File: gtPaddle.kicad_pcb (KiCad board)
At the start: 2 copper layers, 139.7 x 57.2 mm, 24 parts, among them IC1 74157N

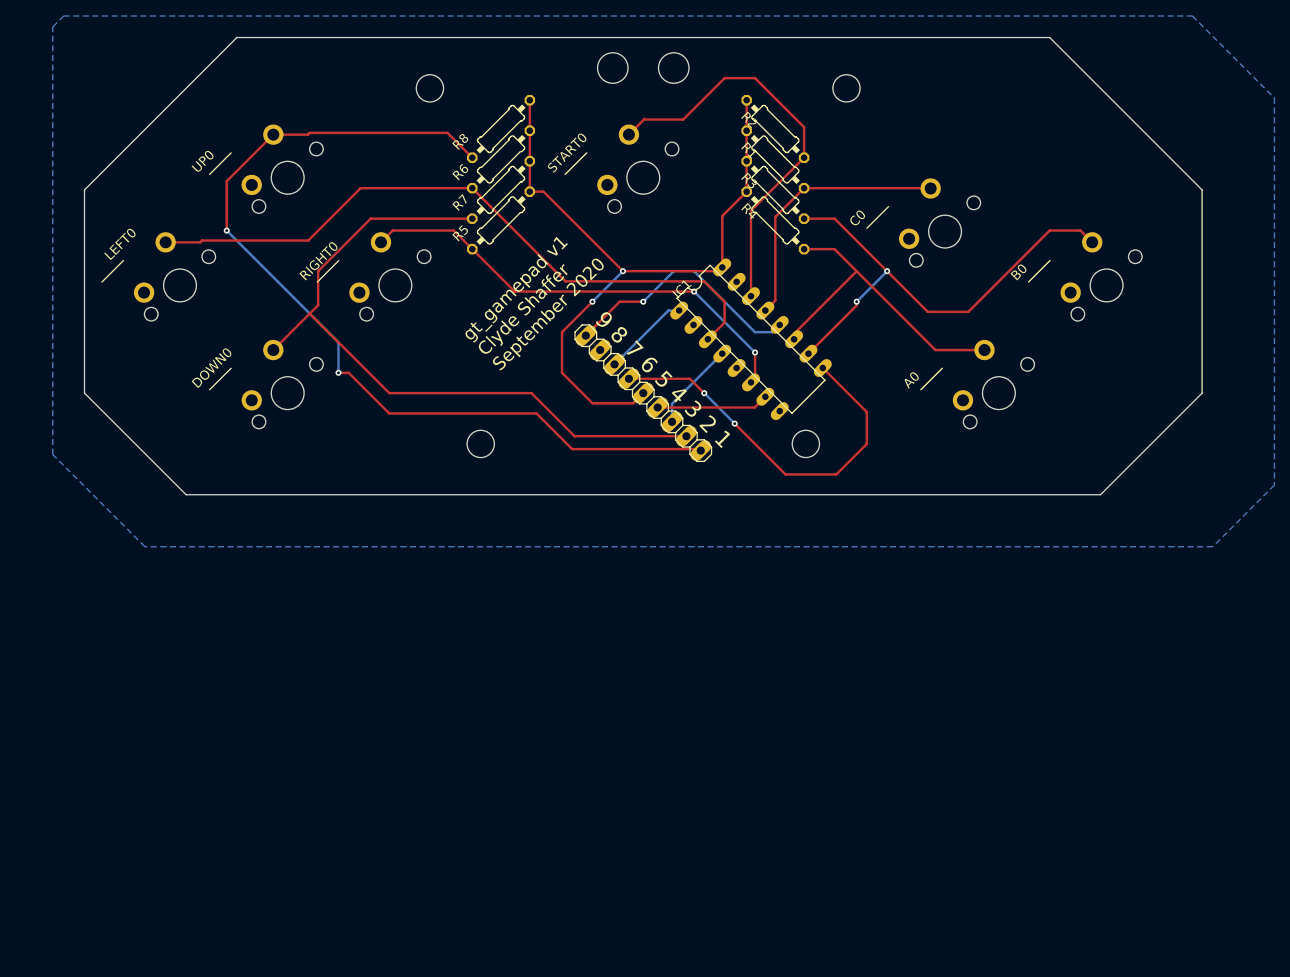
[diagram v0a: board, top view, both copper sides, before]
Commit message: start removing old pcb edits
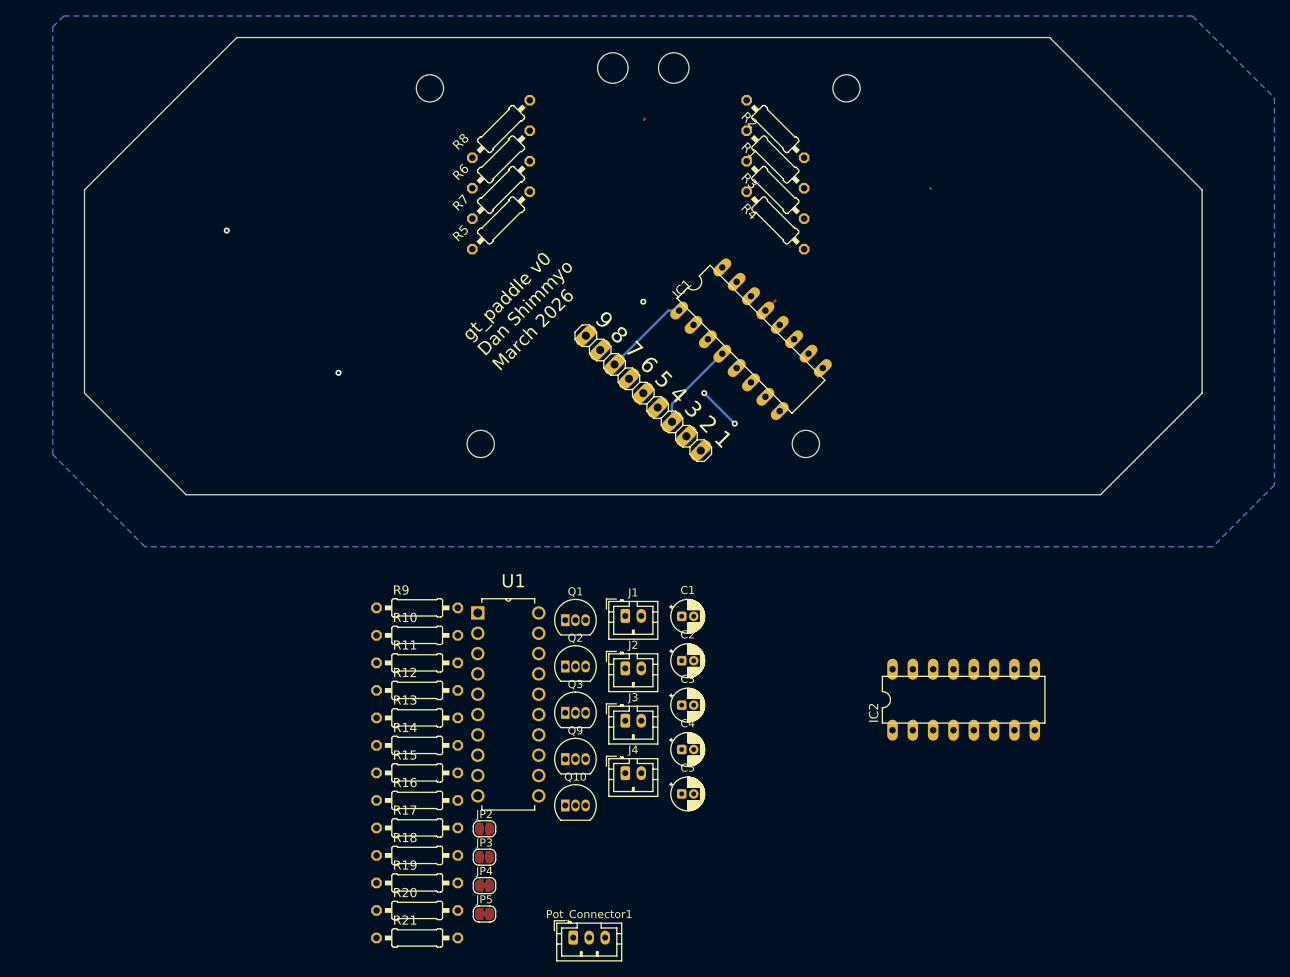
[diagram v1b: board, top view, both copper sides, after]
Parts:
- removed A0, B0, C0, DOWN0, LEFT0, RIGHT0, START0, UP0: CHERRY_MX, gpad1:CHERRY_MX
- added C1: 220pF, Capacitor_THT:CP_Radial_D4.0mm_P1.50mm, F.Cu at (148.4, 139.4)
- added C2: .1µF, Capacitor_THT:CP_Radial_D4.0mm_P1.50mm, F.Cu at (148.4, 144.9)
- added C3: .1µF, Capacitor_THT:CP_Radial_D4.0mm_P1.50mm, F.Cu at (148.4, 150.5)
- added C4: .1µF, Capacitor_THT:CP_Radial_D4.0mm_P1.50mm, F.Cu at (148.4, 156.0)
- added C5: .1µF, Capacitor_THT:CP_Radial_D4.0mm_P1.50mm, F.Cu at (148.4, 161.6)
- added IC2: 74157N, gpad1:DIL16, F.Cu at (183.7, 149.8)
- added J1: Conn_01x02_Pin, Connector_JST:JST_PH_B2B-PH-K_1x02_P2.00mm_Vertical, F.Cu at (141.4, 139.3)
- added J2: Conn_01x02_Pin, Connector_JST:JST_PH_B2B-PH-K_1x02_P2.00mm_Vertical, F.Cu at (141.4, 145.9)
- added J3: Conn_01x02_Pin, Connector_JST:JST_PH_B2B-PH-K_1x02_P2.00mm_Vertical, F.Cu at (141.4, 152.4)
- added J4: Conn_01x02_Pin, Connector_JST:JST_PH_B2B-PH-K_1x02_P2.00mm_Vertical, F.Cu at (141.4, 159.0)
- added JP2: SolderJumper_2_Open, Jumper:SolderJumper-2_P1.3mm_Open_RoundedPad1.0x1.5mm, F.Cu at (123.8, 165.9)
- added JP3: SolderJumper_2_Open, Jumper:SolderJumper-2_P1.3mm_Open_RoundedPad1.0x1.5mm, F.Cu at (123.8, 169.5)
- added JP4: SolderJumper_2_Bridged, Jumper:SolderJumper-2_P1.3mm_Bridged_RoundedPad1.0x1.5mm, F.Cu at (123.8, 173.0)
- added JP5: SolderJumper_2_Bridged, Jumper:SolderJumper-2_P1.3mm_Bridged_RoundedPad1.0x1.5mm, F.Cu at (123.8, 176.6)
- added Pot_Connector1: Conn_01x03_Pin, Connector_JST:JST_PH_B3B-PH-K_1x03_P2.00mm_Vertical, F.Cu at (134.8, 179.5)
- added Q1: 2N3904, Package_TO_SOT_THT:TO-92_Inline, F.Cu at (133.9, 139.9)
- added Q10: 2N3904, Package_TO_SOT_THT:TO-92_Inline, F.Cu at (133.9, 163.0)
- added Q2: 2N3904, Package_TO_SOT_THT:TO-92_Inline, F.Cu at (133.9, 145.7)
- added Q3: 2N3904, Package_TO_SOT_THT:TO-92_Inline, F.Cu at (133.9, 151.4)
- added Q9: 2N3904, Package_TO_SOT_THT:TO-92_Inline, F.Cu at (133.9, 157.2)
- added R10: 1K, gpad1:0207_10, F.Cu at (115.3, 141.8)
- added R11: 10K, gpad1:0207_10, F.Cu at (115.3, 145.2)
- added R12: 10K, gpad1:0207_10, F.Cu at (115.3, 148.6)
- added R13: 1K, gpad1:0207_10, F.Cu at (115.3, 152.1)
- added R14: 10K, gpad1:0207_10, F.Cu at (115.3, 155.5)
- added R15: 3.3K, gpad1:0207_10, F.Cu at (115.3, 159.0)
- added R16: 10K, gpad1:0207_10, F.Cu at (115.3, 162.4)
- added R17: 3.3K, gpad1:0207_10, F.Cu at (115.3, 165.8)
- added R18: 10K, gpad1:0207_10, F.Cu at (115.3, 169.3)
- added R19: 3.3K, gpad1:0207_10, F.Cu at (115.3, 172.7)
- added R20: 3.3K, gpad1:0207_10, F.Cu at (115.3, 176.2)
- added R21: 10K, gpad1:0207_10, F.Cu at (115.3, 179.6)
- added R9: 1K, gpad1:0207_10, F.Cu at (115.3, 138.3)
- added U1: ADC0804LCN, gpad1:DIP254P762X508-20, F.Cu at (130.5, 161.8)
- JP1: value (none) -> PINHD-1X9
- R1, R2, R3, R4: value (none) -> 3.3k
- R5, R6, R7, R8: value (none) -> 1k
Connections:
- IC1 pad 2: GND -> Net-(IC1A-1A)
- IC1 pad 3: N$7 -> Net-(IC1A-1B)
- IC1 pad 5: GND -> Net-(IC1A-2A)
- IC1 pad 6: N$8 -> Net-(IC1A-2B)
- JP1 pad 1: N$1 -> Net-(JP2-B)
- JP1 pad 2: N$2 -> Net-(JP3-B)
- R5 pad 1: N$8 -> Net-(IC2A-4B)
- R6 pad 1: N$7 -> Net-(IC2A-4A)
- R7 pad 1: N$2 -> Net-(IC2A-3B)
- R8 pad 1: N$1 -> Net-(IC2A-3A)
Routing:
- net N$1: track 113.5 -> 0.00 mm, vias 2 -> 0
- net VCC: track 90.1 -> 0.00 mm, vias 2 -> 0
- net N$2: track 87.6 -> 0.00 mm
- net N$7: track 84.1 -> 0.00 mm
- net Net-(IC1A-3B): track 60.0 -> 0.00 mm, vias 2 -> 0
- net N$8: track 57.6 -> 0.00 mm, vias 2 -> 0
- net Net-(IC1A-4A): track 51.4 -> 0.13 mm
- net Net-(IC1A-3Y): track 48.0 -> 5.39 mm
- net Net-(IC1A-3A): track 39.5 -> 0.00 mm
- net Net-(IC1A-4B): track 33.1 -> 1.82 mm
- net Net-(IC1A-4Y): track 31.1 -> 0.00 mm
- net Net-(IC1A-2Y): track 14.0 -> 0.00 mm
- net Net-(JP2-B): vias 0 -> 2
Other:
- board text added: "gt_paddle v0 Dan Shimmyo March 2026"
- board text removed: "gt_gamepad v1 Clyde Shaffer September 2020"

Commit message: start placing mux and adc
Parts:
- moved R2 98.1 mm to (92.9, 149.9), turned to 0 degrees
- moved R8 97.7 mm to (92.9, 170.5), turned to 0 degrees
- moved R3 95.0 mm to (92.9, 153.3), turned to 0 degrees
- moved R4 94.8 mm to (92.9, 156.7), turned to 0 degrees
- moved R1 92.9 mm to (92.9, 146.4), turned to 0 degrees
- moved R6 87.8 mm to (92.9, 163.6), turned to 0 degrees
- moved R7 87.4 mm to (92.9, 167.1), turned to 0 degrees
- moved R5 77.6 mm to (92.9, 160.2), turned to 0 degrees
- moved U1 58.4 mm to (122.5, 104.0), turned to -45 degrees
- moved IC2 48.7 mm to (170.9, 102.8), turned to -45 degrees
- moved IC1 3.51 mm to (154.2, 102.7)
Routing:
- net Net-(IC1A-1Y): track 11.1 -> 0.00 mm
- net Net-(IC1A-~{A}/B): track 10.9 -> 0.00 mm
- net Net-(IC1A-3Y): track 5.39 -> 0.00 mm, vias 2 -> 0
- net Net-(IC1A-4B): track 1.82 -> 0.00 mm
- net Net-(JP2-B): vias 2 -> 0
- net Net-(IC1A-4Y): vias 1 -> 0

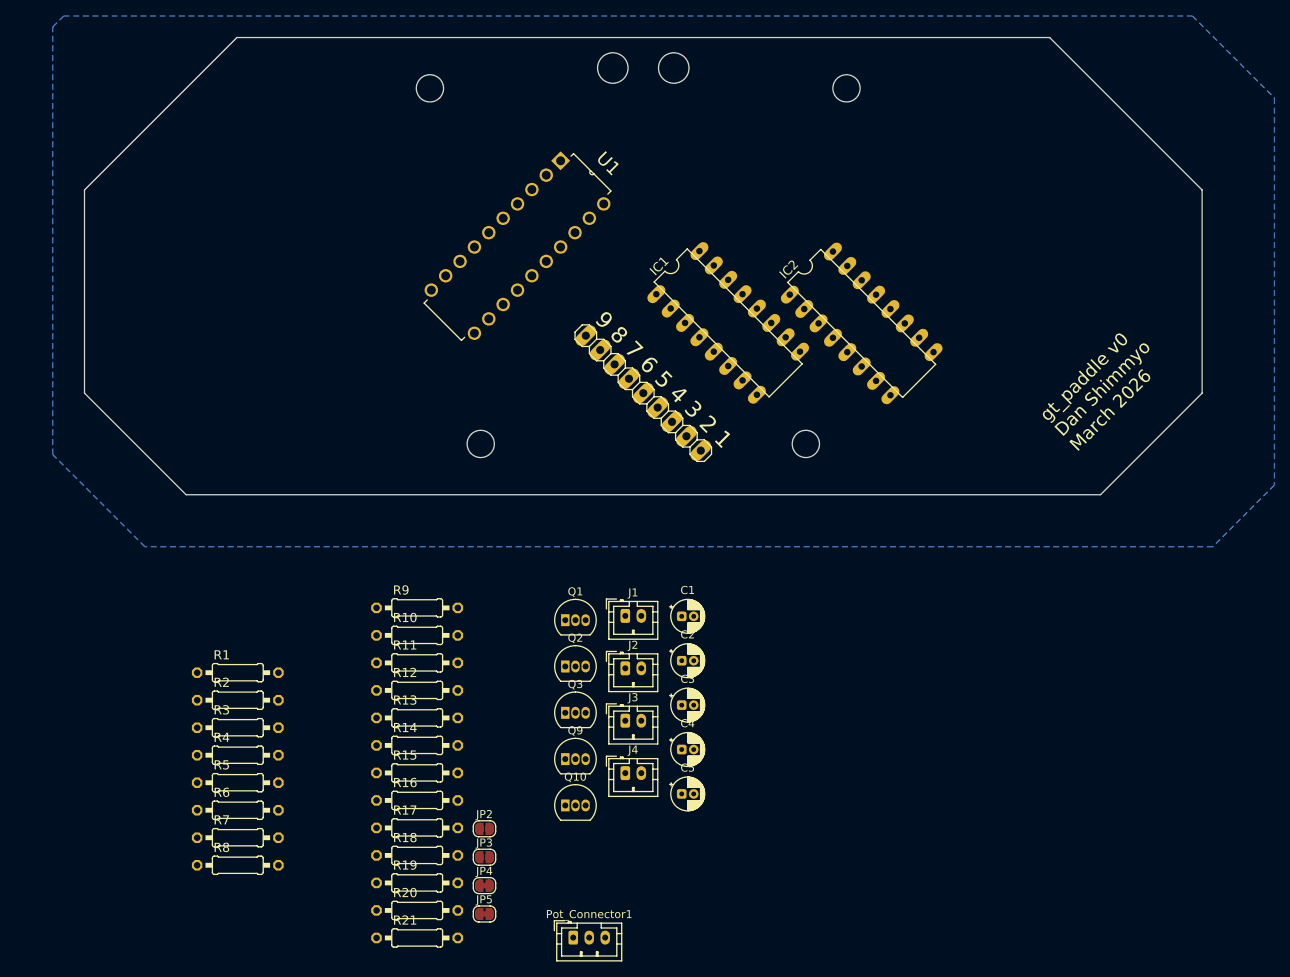
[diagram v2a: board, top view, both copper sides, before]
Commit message: first pass placement no traces
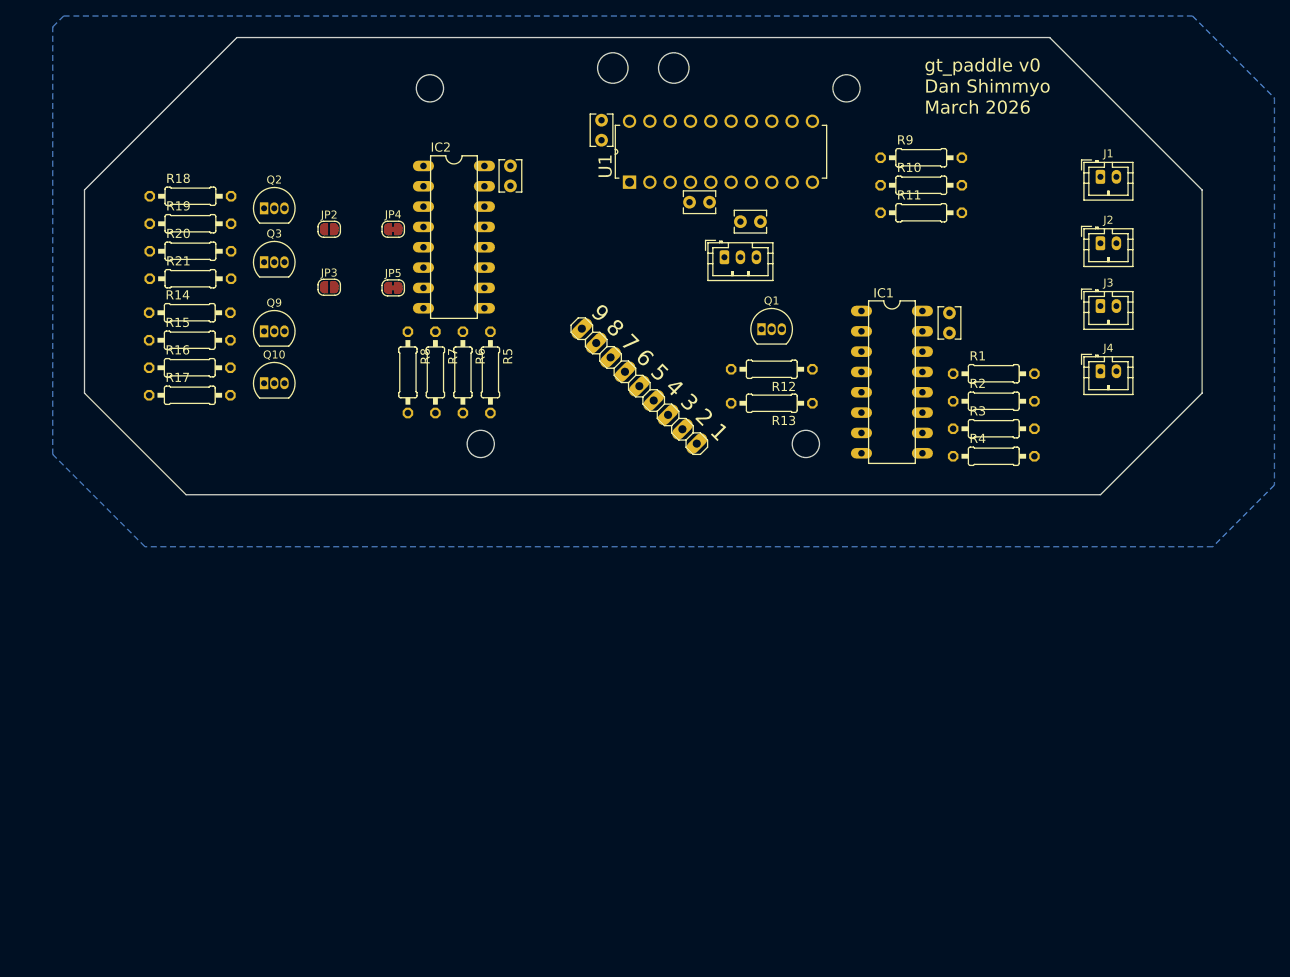
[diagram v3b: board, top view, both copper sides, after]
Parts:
- C1, C2, C3, C4, C5: footprint Capacitor_THT:CP_Radial_D4.0mm_P1.50mm -> Capacitor_THT:C_Disc_D3.8mm_W2.6mm_P2.50mm
- moved R1 101.6 mm to (187.4, 109.1)
- moved R2 101.6 mm to (187.4, 112.5)
- moved R3 101.6 mm to (187.4, 115.9)
- moved R4 101.6 mm to (187.4, 119.4)
- moved R18 87.1 mm to (87.0, 86.9)
- moved R19 87.1 mm to (87.0, 90.3)
- moved R20 87.1 mm to (87.0, 93.8)
- moved R21 87.1 mm to (87.0, 97.2)
- moved Pot_Connector1 87.1 mm to (153.8, 94.5)
- moved C5 84.8 mm to (138.4, 77.4), turned to -90 degrees
- moved R10 84.5 mm to (178.3, 85.5)
- moved R11 84.5 mm to (178.3, 88.9)
- moved R9 84.5 mm to (178.3, 82.1)
- moved JP4 82.8 mm to (112.3, 91.0), turned to 180 degrees
- moved J1 80.9 mm to (200.8, 84.5)
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
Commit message: layout tweaks
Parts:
- moved Q10 6.02 mm to (102.2, 109.8)
- moved Q2 6.02 mm to (102.2, 87.9)
- moved Q3 6.02 mm to (102.2, 94.6)
- moved Q9 6.02 mm to (102.2, 103.3)
- moved R14 6.02 mm to (92.9, 100.9)
- moved R15 6.02 mm to (92.9, 104.4)
- moved R16 6.02 mm to (92.9, 107.8)
- moved R17 6.02 mm to (92.9, 111.2)
- moved R18 6.02 mm to (93.0, 86.4)
- moved R19 6.02 mm to (93.0, 89.8)
- moved R20 6.02 mm to (93.0, 93.2)
- moved R21 6.02 mm to (93.0, 96.7)
- moved JP2 4.26 mm to (108.6, 90.8)
- moved JP3 4.26 mm to (108.6, 98.0)
- moved JP5 0.33 mm to (112.3, 98.0)
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
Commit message: pcb commit before rotating npn mux
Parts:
- moved IC2 3.73 mm to (123.6, 91.5)
- moved Q3 3.73 mm to (105.9, 94.1)
- moved Q9 3.73 mm to (105.9, 102.8)
- moved JP2 3.73 mm to (112.3, 90.3)
- moved JP3 3.73 mm to (112.3, 97.5)
- moved JP4 3.73 mm to (116.0, 90.3)
- moved JP5 3.73 mm to (116.0, 97.5)
- moved Q10 3.73 mm to (105.9, 109.3)
- moved Q2 3.73 mm to (105.9, 87.4)
- moved R14 3.73 mm to (96.6, 100.4)
- moved R15 3.73 mm to (96.6, 103.9)
- moved R16 3.73 mm to (96.6, 107.3)
- moved R17 3.73 mm to (96.6, 110.8)
- moved R18 3.73 mm to (96.7, 85.9)
- moved R19 3.73 mm to (96.7, 89.3)
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
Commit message: tighter layout
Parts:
- R1, R10, R11, R12, R13, R14, R15, R16, R17, R18, R19, R2, R20, R21, R3, R4, R5, R6, R7, R8, R9: footprint gpad1:0207_10 -> Resistor_THT:R_Axial_DIN0309_L9.0mm_D3.2mm_P2.54mm_Vertical
- moved R4 25.1 mm to (173.4, 98.6), turned to 180 degrees
- moved R21 22.2 mm to (114.6, 83.1), turned to -90 degrees
- moved J1 21.0 mm to (179.8, 84.9)
- moved J2 21.0 mm to (179.8, 93.2)
- moved J3 21.0 mm to (179.8, 101.0)
- moved J4 21.0 mm to (179.8, 109.2)
- moved R3 19.2 mm to (173.4, 102.8), turned to 180 degrees
- moved R16 19.2 mm to (114.8, 101.2), turned to -90 degrees
- moved R20 18.4 mm to (110.8, 80.9), turned to -90 degrees
- moved R17 18.0 mm to (111.0, 100.0), turned to -90 degrees
- moved R2 15.1 mm to (173.4, 106.9), turned to 180 degrees
- moved C4 14.4 mm to (171.0, 92.1)
- moved IC1 14.4 mm to (163.8, 100.8)
- moved R1 14.2 mm to (173.4, 111.0), turned to 180 degrees
- moved R19 13.3 mm to (107.0, 80.9), turned to -90 degrees
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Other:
- board text added: "+"
- board text added: "-"

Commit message: edited bjt footprint
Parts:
- Q1, Q10, Q2, Q3, Q9: footprint Package_TO_SOT_THT:TO-92_Inline -> Package_TO_SOT_THT:TO-92S-EBC

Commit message: compact layout
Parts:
- removed @HOLE0, @HOLE1, @HOLE2, @HOLE3: , 
- moved R18 56.4 mm to (124.8, 135.2), turned to 0 degrees
- moved R19 52.8 mm to (122.6, 131.4), turned to 0 degrees
- moved R14 52.0 mm to (142.9, 135.0), turned to 0 degrees
- moved Q9 49.3 mm to (150.8, 131.5), turned to 180 degrees
- moved Q2 48.2 mm to (132.6, 131.6), turned to 180 degrees
- moved R20 48.1 mm to (122.6, 127.6), turned to 0 degrees
- moved R15 46.5 mm to (141.7, 131.2), turned to 0 degrees
- moved Q3 43.5 mm to (130.0, 127.4), turned to 0 degrees
- moved Q10 42.4 mm to (148.3, 127.2), turned to 0 degrees
- moved R21 41.9 mm to (124.8, 123.8), turned to 0 degrees
- moved R17 41.1 mm to (141.7, 127.4), turned to 0 degrees
- moved JP2 36.7 mm to (131.7, 122.9), turned to 90 degrees
- moved J1 36.0 mm to (156.8, 112.6)
- moved R16 35.9 mm to (142.9, 123.6), turned to 0 degrees
- moved JP3 34.7 mm to (138.9, 122.9), turned to 90 degrees
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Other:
- board size 139.7 x 57.2 mm -> 60.6 x 72.6 mm
